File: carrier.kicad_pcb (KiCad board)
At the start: 4 copper layers, 30 x 48 mm, 25 parts, among them J1 Conn_02x06_Odd_Even, J2 DB15_Female_HighDensity, J3 USB_B_Micro, SW1 SW_Push_hrs, SW2 SW_Push_min, SW3 SW_Push_sec, U1 CARAVEL, U2 W25Q128JVS, U5 LP5907MFX-1.8, U6 LP5907MFX-3.3, X1 SG-5032CAN

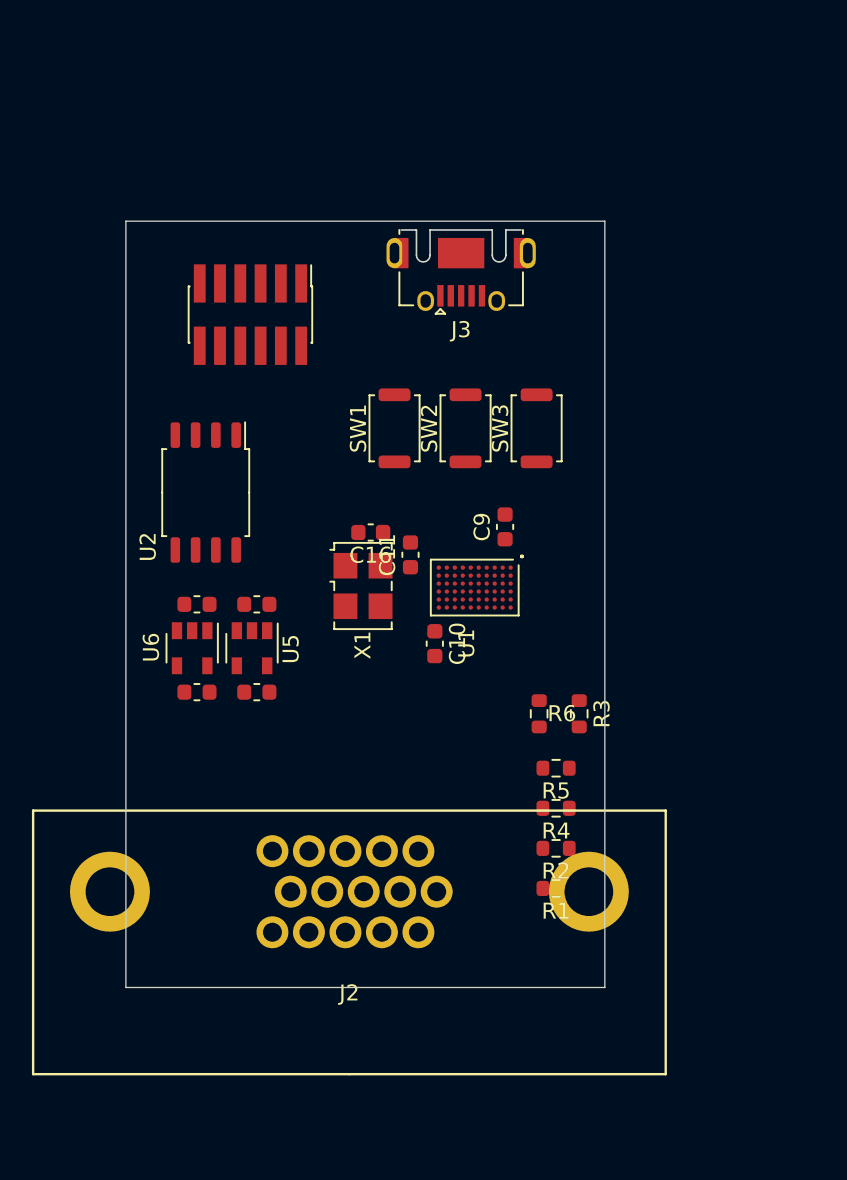
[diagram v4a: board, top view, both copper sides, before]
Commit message: docs and license. fix db15 fp, add oshw logo
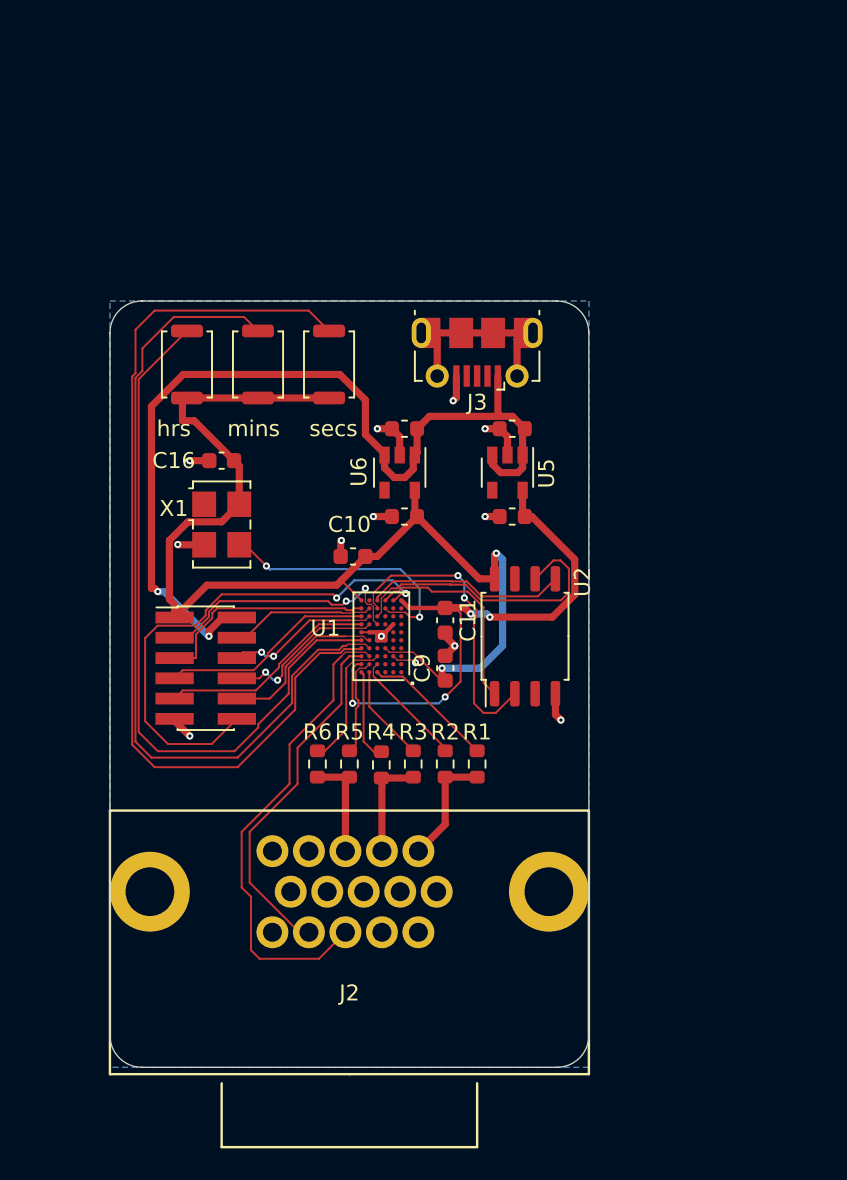
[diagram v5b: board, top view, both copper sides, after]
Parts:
- added G***: LOGO, carrier:oshw-logo-small, B.Cu at (41.9, 70.0)
- J3: footprint Connector_USB:USB_Micro-AB_Molex_47590-0001 -> Connector_USB:USB_Micro-B_Molex-105017-0001
- moved J1 22.3 mm to (40.7, 83.0), turned to 0 degrees
- moved U2 21.9 mm to (60.7, 81.0), turned to 90 degrees
- moved C1 19.4 mm to (59.9, 68.0)
- moved C3 19.4 mm to (59.9, 73.5)
- moved U5 19.4 mm to (59.6, 70.8)
- moved C5 17.0 mm to (53.2, 68.0)
- moved C7 17.0 mm to (53.2, 73.5)
- moved U6 17.0 mm to (52.9, 70.8)
- moved R6 14.2 mm to (47.7, 89.0), turned to 90 degrees
- moved SW1 13.6 mm to (39.6, 64.0), turned to 270 degrees
- moved SW2 13.6 mm to (44.0, 64.0), turned to 270 degrees
- moved SW3 13.6 mm to (48.5, 64.0), turned to 270 degrees
- moved R5 12.9 mm to (49.7, 89.0), turned to 90 degrees
- moved R4 11.3 mm to (51.7, 89.1), turned to 90 degrees
- moved R3 10.9 mm to (53.7, 89.0), turned to 90 degrees
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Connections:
- J2 pad 13: /hsync -> mprj_io[11]
- J2 pad 14: /vsync -> mprj_io[12]
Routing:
- net vdda: track 0.00 -> 73.0 mm, vias 0 -> 2
- net +5V: track 0.00 -> 59.3 mm, vias 0 -> 2
- net mprj_io[10]: track 0.00 -> 58.4 mm
- net mprj_io[9]: track 0.00 -> 52.3 mm
- net mprj_io[8]: track 0.00 -> 44.8 mm
- net vccd: track 0.00 -> 35.0 mm, vias 0 -> 4
- net resetb: track 0.00 -> 32.7 mm, vias 0 -> 2
- net mprj_io[11]: track 0.00 -> 30.0 mm
- net GND: track 0.00 -> 24.3 mm, vias 0 -> 13
- net mprj_io[12]: track 0.00 -> 22.5 mm
- net flash_io1: track 0.00 -> 18.7 mm, vias 0 -> 2
- net flash_clk: track 0.00 -> 18.2 mm
- net clock: track 0.00 -> 16.6 mm, vias 0 -> 2
- net mprj_io[0]: track 0.00 -> 16.3 mm, vias 0 -> 2
- net mprj_io[2]: track 0.00 -> 14.1 mm
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- added copper zone on B.Cu, net GND
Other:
- outline, holes or cut-outs redrawn
- board text added: "ASIC VGA Clock"
- board text added: "Matt Venn 2021"
- board text added: "Serial number"
- board text added: "boards by OSHPark.com"
- board text added: "hrs"
- board text added: "mins"
- board text added: "open source ASIC, PCB & Firmware"
- board text added: "secs"

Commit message: routing and silk improvements, added an led to GPIO
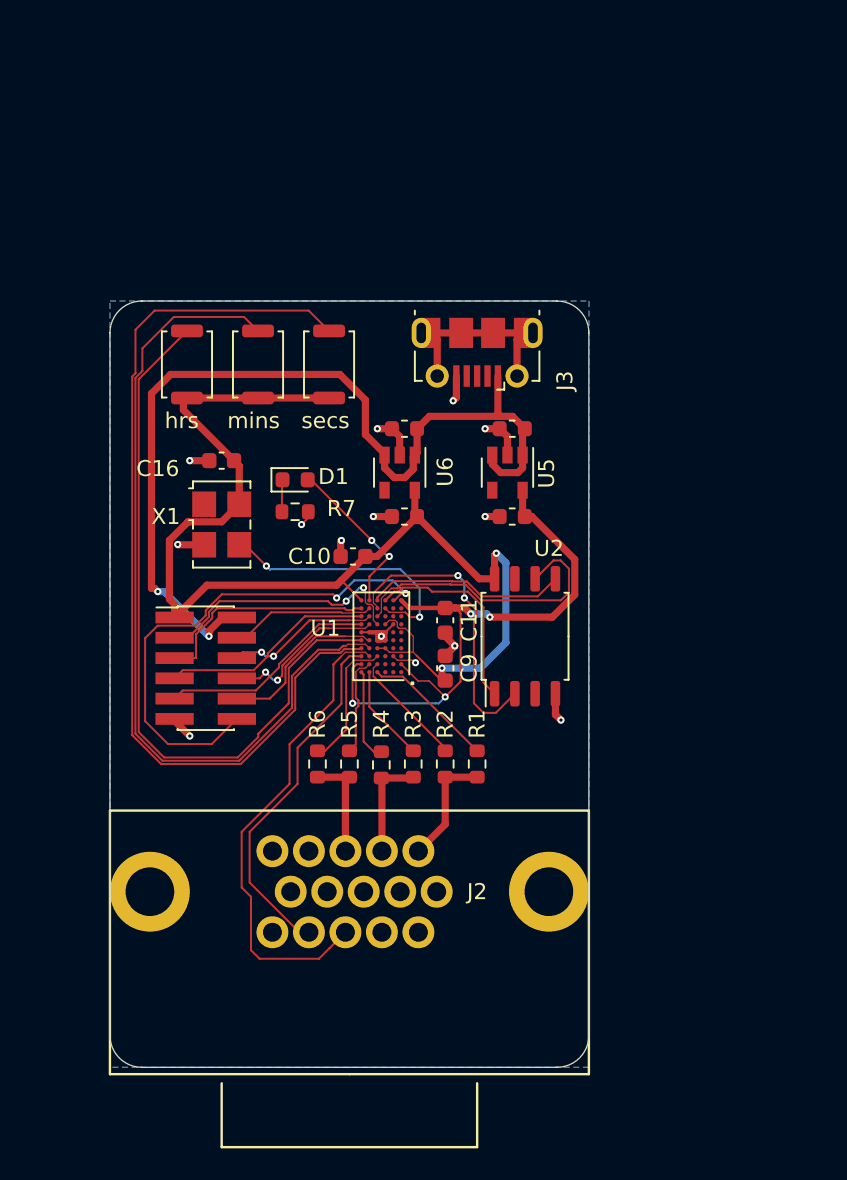
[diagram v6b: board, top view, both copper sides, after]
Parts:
- removed G***: LOGO, carrier:oshw-logo-small
- added D1: LED, LED_SMD:LED_0603_1608Metric, F.Cu at (46.3, 71.2)
- added R7: R, Resistor_SMD:R_0603_1608Metric, F.Cu at (46.3, 73.2)
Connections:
- U1 pad A2: Net-(U1-PadA2) -> vccd
- U1 pad C7: Net-(U1-PadC7) -> vdda
- U1 pad D4: Net-(U1-PadD4) -> vdda
- U1 pad E10: Net-(U1-PadE10) -> gpio
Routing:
- net gpio: track 0.00 -> 10.4 mm, vias 0 -> 2
- net vdda: track 73.0 -> 76.7 mm
- net vccd: track 35.0 -> 38.6 mm
- net Net-(D1-Pad1): track 0.00 -> 2.02 mm
- net GND: track 24.3 -> 25.9 mm, vias 13 -> 14
- net mprj_io[8]: track 44.8 -> 45.4 mm
- net mprj_io[10]: track 58.4 -> 57.9 mm
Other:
- copper layers 4 -> 2

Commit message: continue to tweak layout
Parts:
- added G***: LOGO, carrier:oshw-logo-small, B.Cu at (41.8, 70.1)

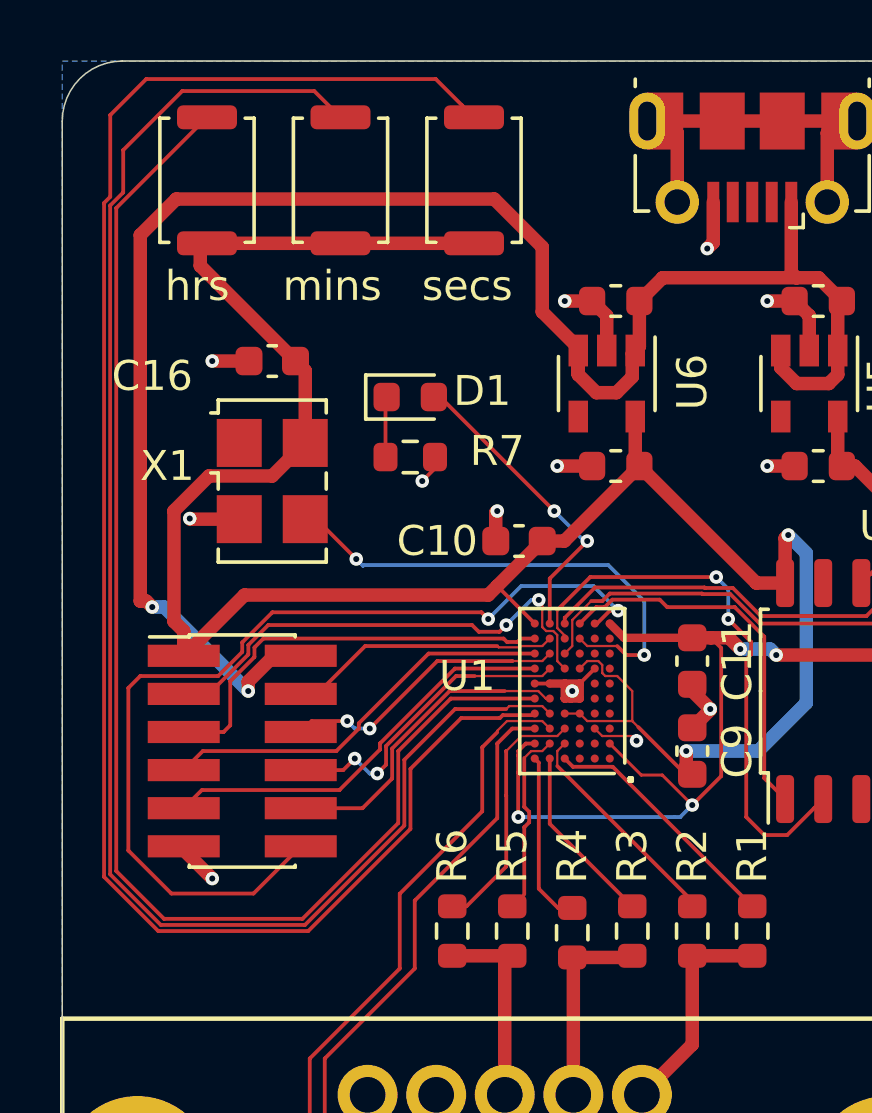
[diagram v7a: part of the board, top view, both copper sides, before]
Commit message: all BOM parts found on digikey, button footprint
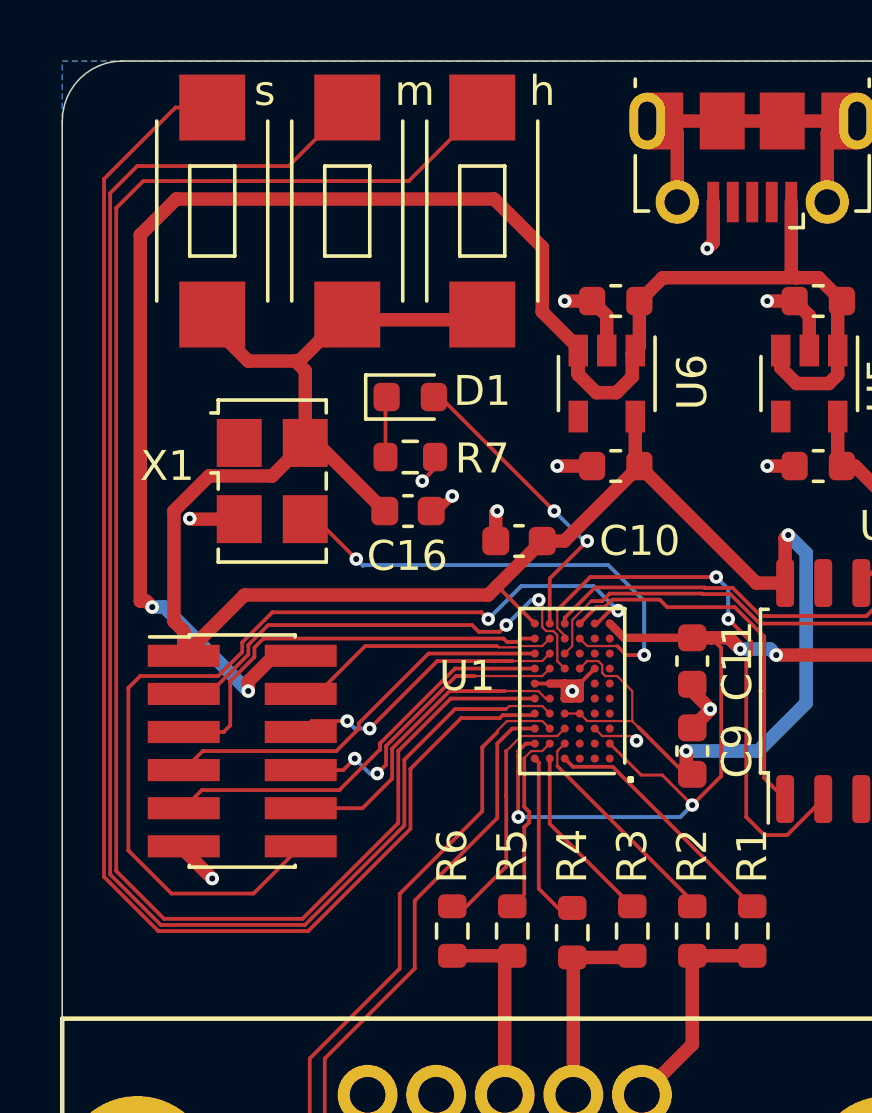
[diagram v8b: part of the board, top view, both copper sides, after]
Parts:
- C1, C5: value 1u -> 1u 16v
- C3, C7: value 4u7 -> 4u7 16v
- R1, R3, R5: value R -> 500R
- R2, R4, R6: value R -> 1k
- R7: value R -> 100R
- SW1, SW2, SW3: footprint Button_Switch_SMD:SW_Push_SPST_NO_Alps_SKRK -> carrier:pts636
- U2: value W25Q128JVS -> W25Q32JVSSIQ-TR
- U5: value LP5907MFX-1.8 -> MCP1824T-1802E/OT
- U6: value LP5907MFX-3.3 -> MIC5504-3.3YM5-TR
- X1: value SG-5032CAN -> ECS-5032MV-100-BN-TR
- moved SW1 9.23 mm to (48.7, 65.0)
- moved SW3 8.79 mm to (39.7, 65.0)
- moved C16 6.74 mm to (46.3, 75.0), turned to 0 degrees
- moved SW2 1.05 mm to (44.2, 65.0)
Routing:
- net mprj_io[10]: track 57.9 -> 47.1 mm
- net mprj_io[8]: track 45.4 -> 54.7 mm
- net mprj_io[9]: track 52.5 -> 51.6 mm
- net vdda: track 76.7 -> 76.1 mm
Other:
- board text added: "h"
- board text added: "m"
- board text added: "s"
- board text removed: "hrs"
- board text removed: "mins"
- board text removed: "secs"
